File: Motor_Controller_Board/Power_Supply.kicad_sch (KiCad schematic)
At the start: 25 parts, among them J202 Conn_01x02, U204 LM2596S-ADJ, U205 LM2596S-ADJ, U206 LM2596S-ADJ

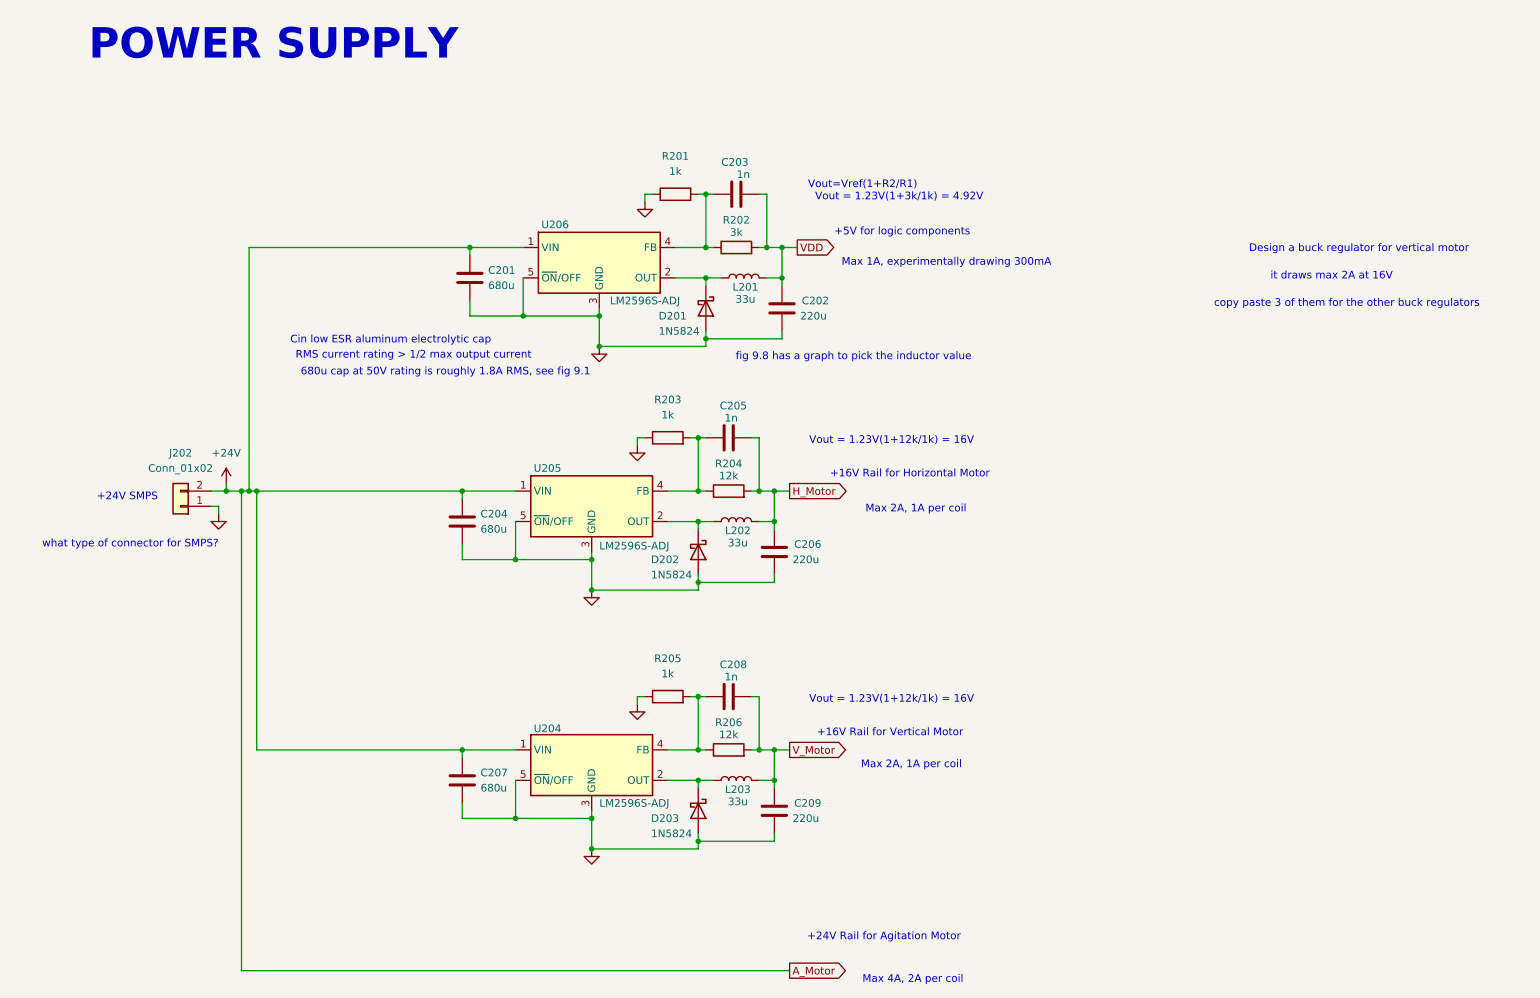
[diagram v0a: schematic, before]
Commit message: picking footprints. still need buck regulator footprints
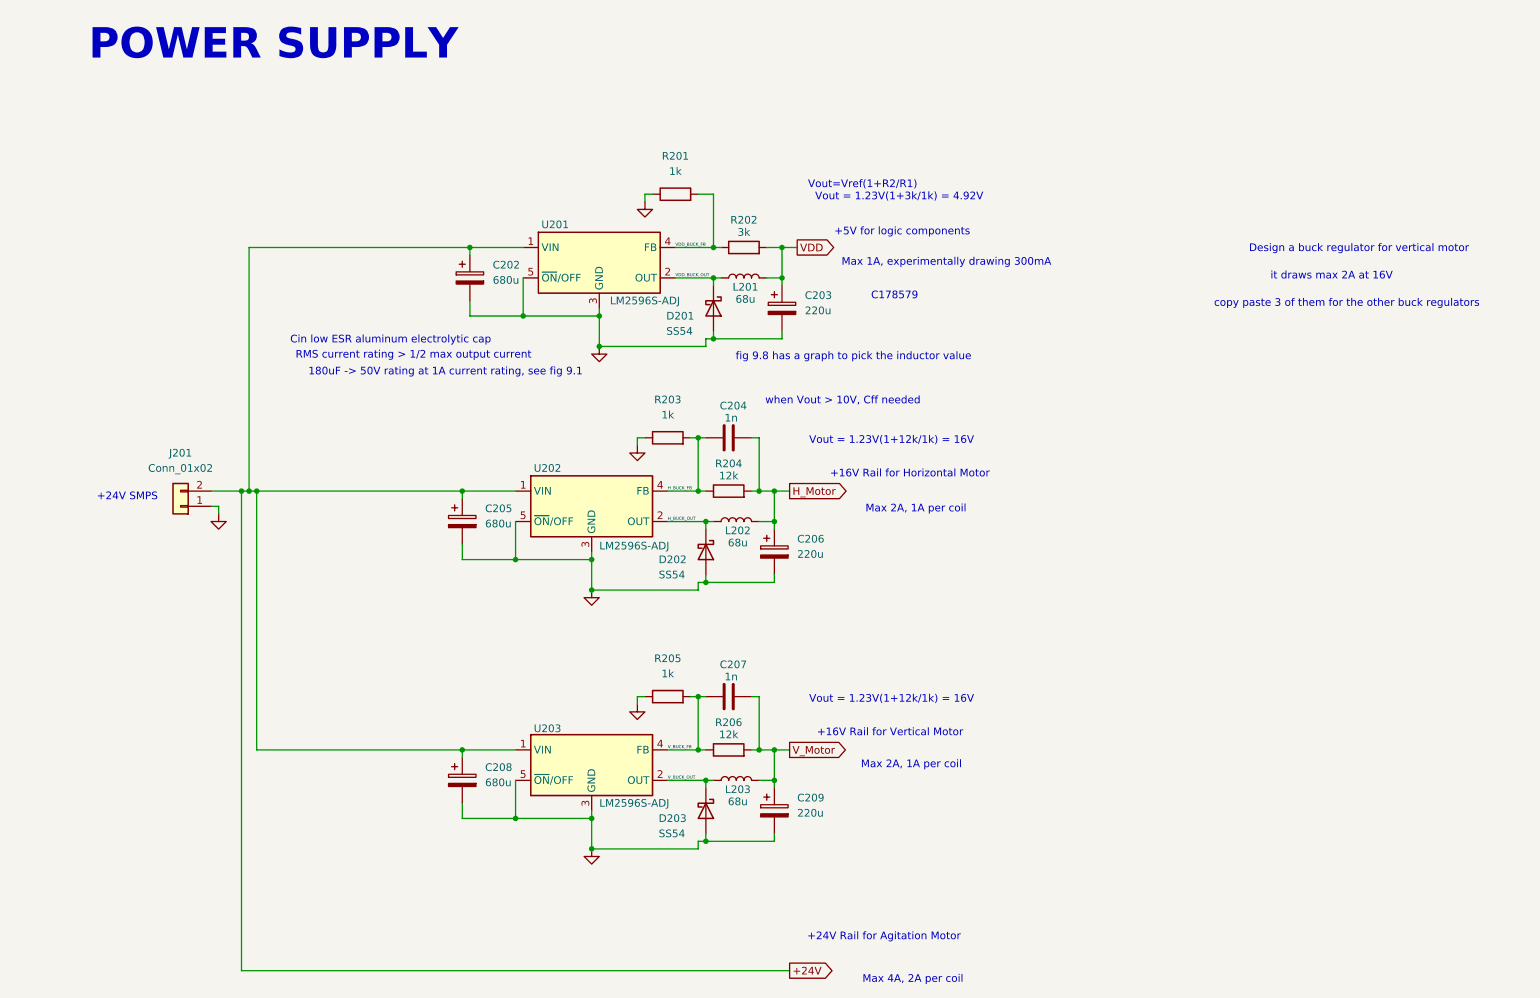
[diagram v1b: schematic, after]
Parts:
- removed C201, C204, C207: 680u, symbol Device:C
- removed C202, C206, C209: 220u, symbol Device:C
- removed C203: 1n, symbol Device:C
- added C202, C205, C208: 680u, symbol Device:C_Polarized
- added C203, C206, C209: 220u, symbol Device:C_Polarized
- D201, D202, D203: value 1N5824 -> SS54; footprint (none) -> Diode_SMD:D_SMA
- J201: renamed from J202; footprint (none) -> TerminalBlock:TerminalBlock_bornier-2_P5.08mm
- L201, L202, L203: value 33u -> 68u
- R201, R202, R203, R204, R205, R206: footprint (none) -> Resistor_SMD:R_0603_1608Metric
- renumbered C205 to C204, C208 to C207, U206 to U201, U205 to U202, U204 to U203
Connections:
- net +24V: now also C202.1, C205.1, C208.1
- net GND: now also C202.2, C203.2, C205.2, C206.2, C208.2, C209.2
- net H_Motor: now also C206.1
- net VDD: now also C203.1
- net V_Motor: now also C209.1
- net H_BUCK_OUT: now reaches D202.1 (K), L202.1, U202.2 (OUT)
- net V_BUCK_FB: now reaches C207.1, R205.2, R206.1, U203.4 (FB)
- net VDD_BUCK_OUT: now reaches D201.1 (K), L201.1, U201.2 (OUT)
- net VDD_BUCK_FB: now reaches R201.2, R202.1, U201.4 (FB)
- net H_BUCK_FB: now reaches C204.1, R203.2, R204.1, U202.4 (FB)
- net V_BUCK_OUT: now reaches D203.1 (K), L203.1, U203.2 (OUT)
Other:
- note added: "180uF -> 50V rating at 1A current rating, see fig 9.1"
- note added: "C178579"
- note added: "when Vout > 10V, Cff needed"
- note removed: "680u cap at 50V rating is roughly 1.8A RMS, see fig 9.1"
- note removed: "what type of connector for SMPS?"
- moved on the sheet: D203, R202

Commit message: schematic and footprints have been selected. ready to start layout, but always open to changes in schematic
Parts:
- C202, C205, C208: value 680u -> 220u; footprint (none) -> Capacitor_SMD:C_Elec_10x10.2; LCSC Part Number (none) -> C178579; MPN (none) -> EEEFP1H221AP; Manufacturer (none) -> PANASONIC
- C203: footprint (none) -> Capacitor_SMD:C_Elec_10x10.2
- C204, C207: footprint (none) -> Capacitor_SMD:C_0603_1608Metric; JCSC Part Number (none) -> C1588; MPN (none) -> CL10B102KB8NNNC; Manufacturer (none) -> Samsung Electro-Mechanics
- C206, C209: footprint (none) -> Capacitor_SMD:C_Elec_10x10.2; LCSC Part Number (none) -> C178579; MPN (none) -> EEEFP1H221AP; Manufacturer (none) -> PANASONIC
- L201, L202, L203: value 68u -> 47u; footprint (none) -> Inductor_SMD:L_12x12mm_H8mm; JCSC Part Number (none) -> C9906; MPN (none) -> SMDRI127-470MT; Manufacturer (none) -> SXN(Shun Xiang Nuo Elec)
- R201: JCSC Part Number (none) -> C21190; MPN (none) -> 0603WAF1001T5E; Manufacturer (none) -> UNI-ROYAL(Uniroyal Elec)
- R202: JCSC Part Number (none) -> C4211; MPN (none) -> 0603WAF3001T5E; Manufacturer (none) -> UNI-ROYAL(Uniroyal Elec)
- R204, R206: JCSC Part Number (none) -> C22790; MPN (none) -> 0603WAF1202T5E; Manufacturer (none) -> UNI-ROYAL(Uniroyal Elec)
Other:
- moved on the sheet: J201

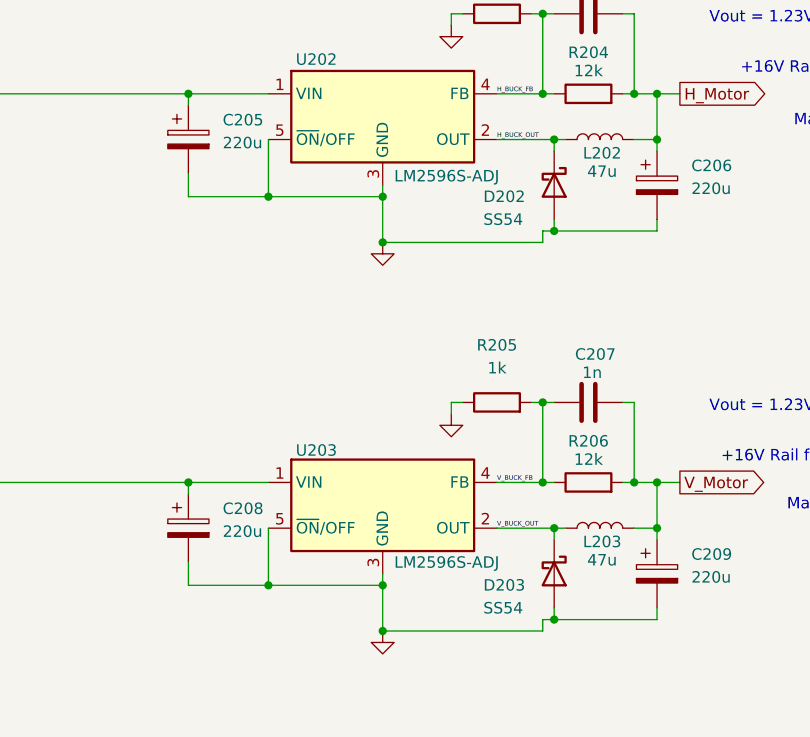
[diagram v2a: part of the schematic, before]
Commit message: changed jcsc to lcsc
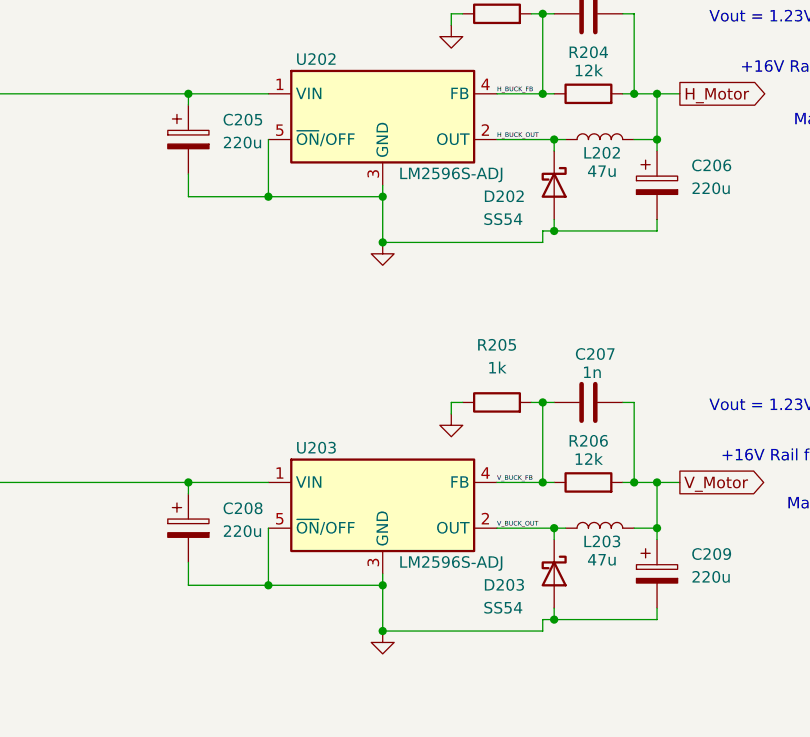
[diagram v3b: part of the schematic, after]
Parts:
- C204, C207: JCSC Part Number C1588 -> (none); LCSC Part Number (none) -> C1588
- D201, D202, D203: LCSC Part Number (none) -> C22452; MPN (none) -> SS54; Manufacturer (none) -> MDD(Microdiode Semiconductor)
- J201: now left out of the parts list
- L201, L202, L203: JCSC Part Number C9906 -> (none); LCSC Part Number (none) -> C9906
- R201: JCSC Part Number C21190 -> (none); LCSC Part Number (none) -> C21190
- R202: JCSC Part Number C4211 -> (none); LCSC Part Number (none) -> C4211
- R203, R205: LCSC Part Number (none) -> C21190; MPN (none) -> 0603WAF1001T5E; Manufacturer (none) -> UNI-ROYAL(Uniroyal Elec)
- R204, R206: JCSC Part Number C22790 -> (none); LCSC Part Number (none) -> C22790
- U201, U202, U203: LCSC Part Number (none) -> C29781; MPN (none) -> LM2596SX-ADJ/NOPB; Manufacturer (none) -> Texas Instruments
